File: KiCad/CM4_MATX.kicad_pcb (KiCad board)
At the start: 2 copper layers, 243.8 x 243.8 mm, 66 parts, among them IC1 USB2517-JZX, IC2 PI7C9X2G404SLBFDE, IC3 M24C04-RMN6TP, J1 72309-8014BLF, J10 72309-8014BLF, J11 10104110-0001LF, J12 SS-52100-002, J13 PCIe_x16, J14 PCIe_x16, J15 PCIe_x16, J16 GSD090012SEU, J17 Conn_02x04_Odd_Even, J18 ARJM11C7-502-AB-ER2-T, J19 Conn_02x20_Odd_Even, J20 Conn_02x04_Odd_Even, J3 Conn_01x22_Female, J5 Conn_01x22_Female, J6 1888811-1, J7 39-28-1243, J9 Conn_02x05_Odd_Even, M1 Fan_CPU_4pin, M2 Fan_CPU_4pin, U1 MAX6639ATE+, U10 MIC2019YM6-TR, U11 MIC2019YM6-TR, U12 MIC2019YM6-TR, U13 MIC2019YM6-TR, U14 MIC2019YM6-TR, U15 MIC2019YM6-TR, U16 MIC2019YM6-TR, U17 TCA9548ARGER, U18 PCF85263AT, U19 AP7363-10D, U3 FSUSB42MUX, U4 AP7363-10D, U5 AP2822CKETR-G1, U6 74LVC1G07GW, U7 TPD4EUSB30, U8 RT9742GGJ5, U9 TPD4EUSB30, Y2 Crystal

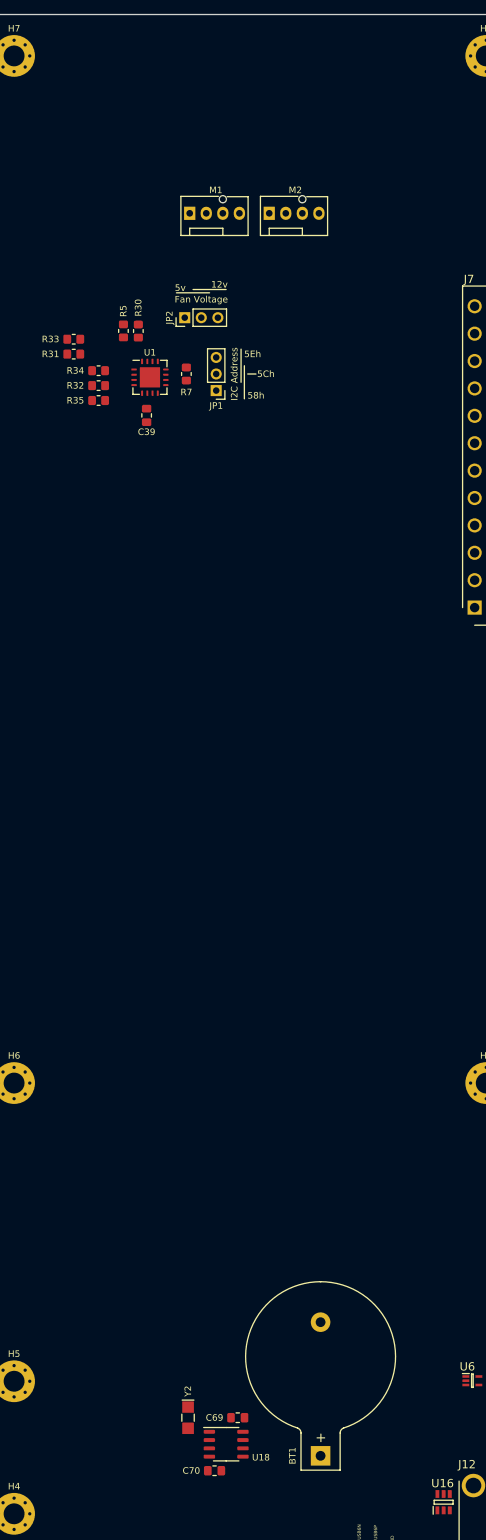
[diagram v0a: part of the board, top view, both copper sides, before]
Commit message: added first wiring of RTC and FAN_CTRL
widths have to be revisited
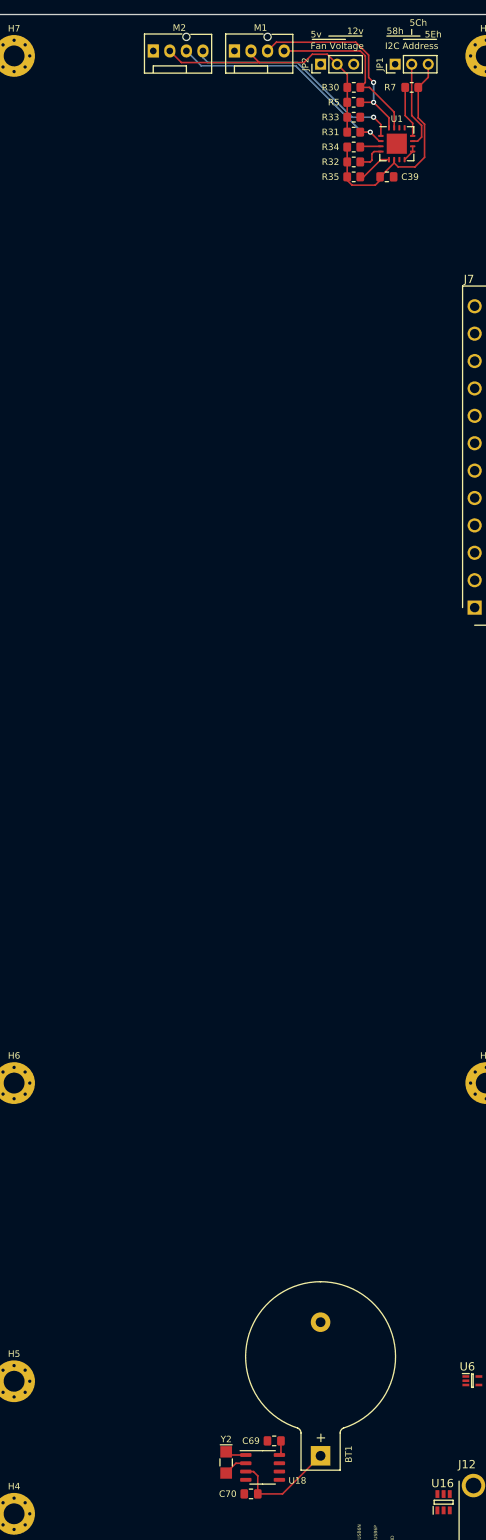
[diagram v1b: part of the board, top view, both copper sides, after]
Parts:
- moved JP1 57.1 mm to (261.6, 30.5), turned to 90 degrees
- moved R7 55.9 mm to (264.2, 34.0), turned to 0 degrees
- moved R31 54.8 mm to (255.3, 40.9)
- moved R33 54.8 mm to (255.3, 38.6)
- moved U1 52.1 mm to (261.9, 42.7)
- moved R32 52.0 mm to (255.3, 45.5)
- moved R34 52.0 mm to (255.3, 43.2)
- moved R35 52.0 mm to (255.3, 47.8)
- moved C39 51.9 mm to (260.4, 47.8), turned to 0 degrees
- moved R30 49.9 mm to (255.3, 34.0), turned to 0 degrees
- moved R5 49.8 mm to (255.3, 36.3), turned to 0 degrees
- moved JP2 44.1 mm to (250.2, 30.5)
- moved M2 30.6 mm to (224.5, 28.4)
- moved M1 25.8 mm to (237.0, 28.4)
- moved Y2 9.01 mm to (235.7, 244.9)
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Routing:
- net /FanCTRL_MAX6639/V_FAN: track 0.00 -> 41.2 mm
- net /FanCTRL_MAX6639/TACH2: track 0.00 -> 37.1 mm, vias 0 -> 1
- net +3V3: track 0.00 -> 35.7 mm
- net /FanCTRL_MAX6639/PWM2: track 0.00 -> 34.6 mm, vias 0 -> 1
- net /FanCTRL_MAX6639/TACH1: track 0.00 -> 31.4 mm, vias 0 -> 2
- net /FanCTRL_MAX6639/PWM1: track 0.00 -> 27.1 mm
- net /RTC_PCF85263A/VBAT: track 0.00 -> 16.9 mm
- net /FanCTRL_MAX6639/ADD: track 0.00 -> 13.4 mm
- net /FanCTRL_MAX6639/~ALERT: track 0.00 -> 7.91 mm
- net /FanCTRL_MAX6639/~OT: track 0.00 -> 5.50 mm
- net /FanCTRL_MAX6639/~THERM: track 0.00 -> 4.42 mm
- net /RTC_PCF85263A/OSCO: track 0.00 -> 3.63 mm
- net /RTC_PCF85263A/OSCI: track 0.00 -> 3.21 mm
- net /FanCTRL_MAX6639/~FANFAIL: track 0.00 -> 3.21 mm
- net /FanCTRL_MAX6639/DX: track 0.00 -> 2.55 mm
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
